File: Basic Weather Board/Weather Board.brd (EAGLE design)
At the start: 160 x 100 mm, 4 parts, among them U1 AT30TS75, U2 TMP101", U3 LPS331AP, U4 MPL3115A2

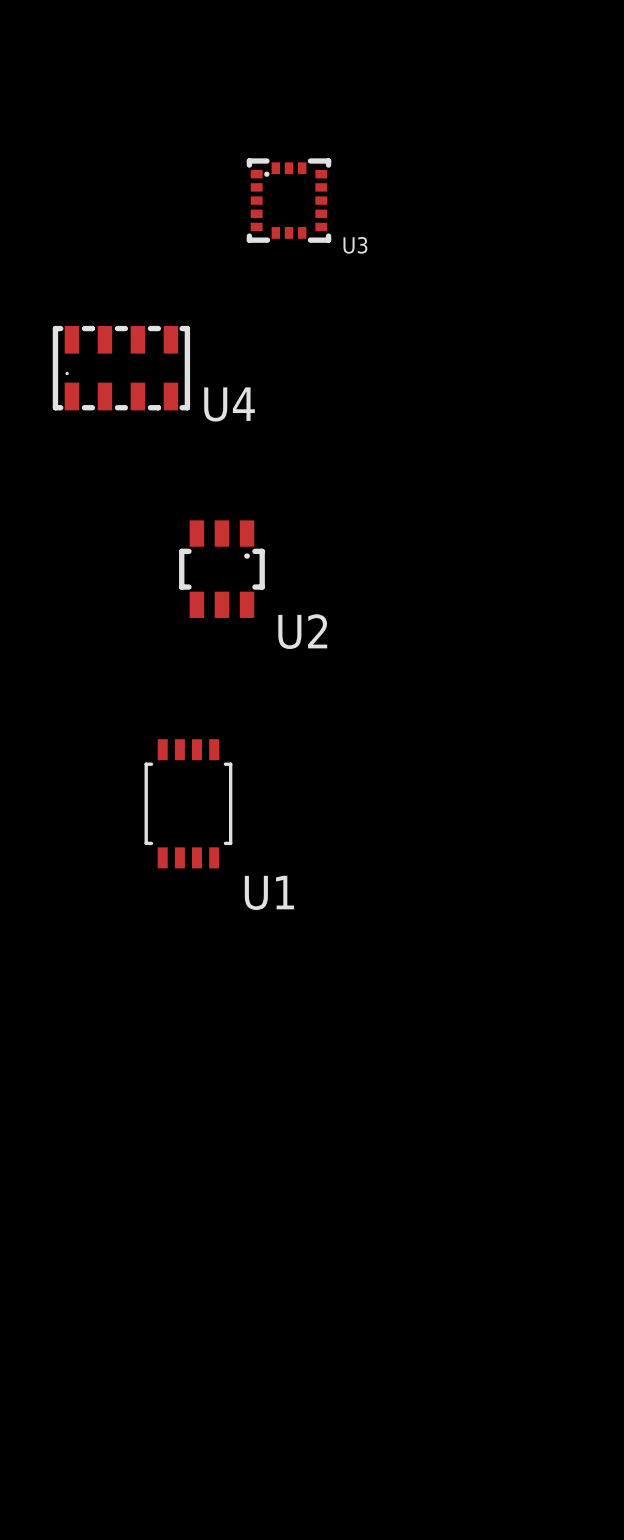
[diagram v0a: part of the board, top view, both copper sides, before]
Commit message: FRDM-KL25Z: Corrected parts to use Newark approved components and added missing componnets
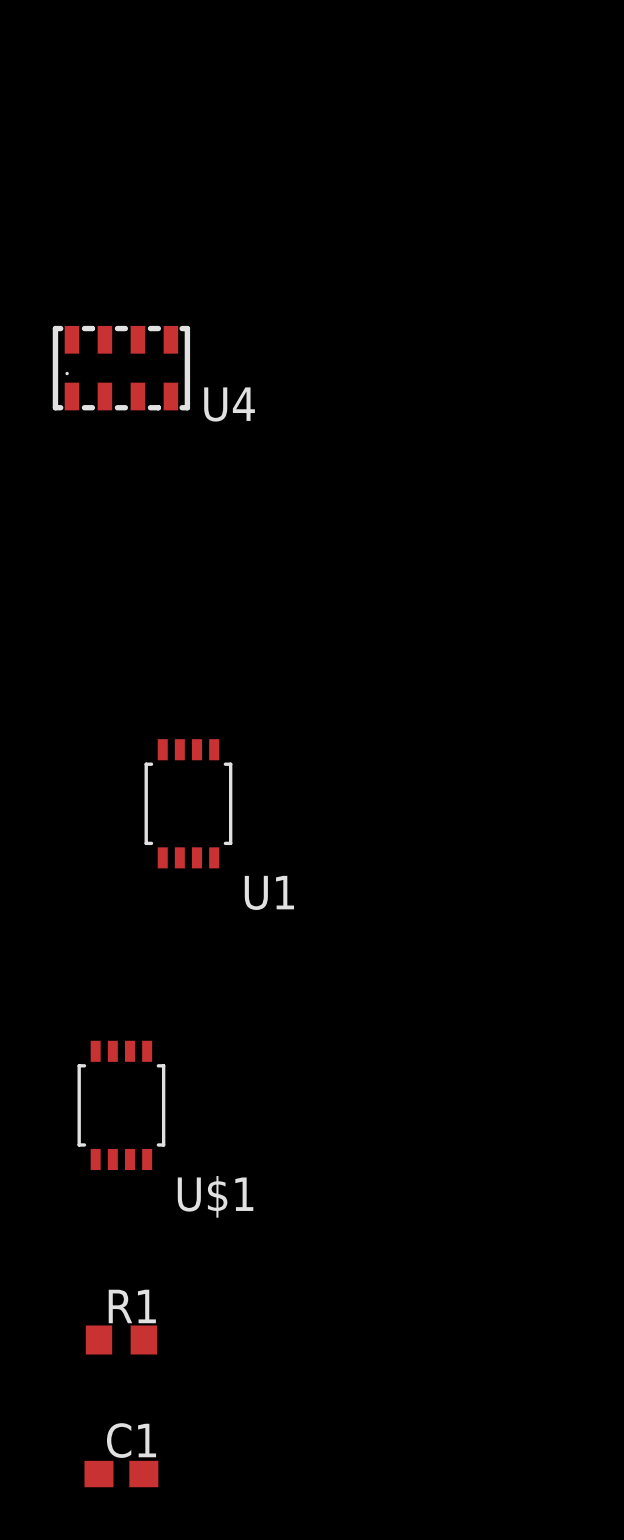
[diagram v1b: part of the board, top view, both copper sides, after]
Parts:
- removed U2: TMP101", Kas-Sensors:SOT23-6
- removed U3: LPS331AP, Kas-Sensors:LGA-16(3X3)
- added C1: 0.1uF, Kas-Capacitors:C0603
- added R1: 10k, Kas-Resistors:R0603
- added U$1: STCN75DS2F, Kas-Sensors:MSOP-8
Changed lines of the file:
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@@
 <layer number="48" name="Document" color="7" fill="1" visible="yes" active="yes"/>
 <layer number="49" name="Reference" color="7" fill="1" visible="yes" active="yes"/>
+<layer number="50" name="dxf" color="7" fill="1" visible="no" active="no"/>
 <layer number="51" name="tDocu" color="7" fill="1" visible="yes" active="yes"/>
 <layer number="52" name="bDocu" color="7" fill="1" visible="yes" active="yes"/>
+<layer number="53" name="tGND_GNDA" color="7" fill="9" visible="no" active="no"/>
+<layer number="54" name="bGND_GNDA" color="1" fill="9" visible="no" active="no"/>
+<layer number="56" name="wert" color="7" fill="1" visible="no" active="no"/>
 <layer number="91" name="Nets" color="2" fill="1" visible="no" active="no"/>
 <layer number="92" name="Busses" color="1" fill="1" visible="no" active="no"/>
@@
 <layer number="97" name="Info" color="7" fill="1" visible="no" active="no"/>
 <layer number="98" name="Guide" color="6" fill="1" visible="no" active="no"/>
+<layer number="100" name="Muster" color="7" fill="1" visible="no" active="no"/>
+<layer number="101" name="Patch_Top" color="12" fill="4" visible="no" active="yes"/>
+<layer number="102" name="Vscore" color="7" fill="1" visible="no" active="yes"/>
+<layer number="103" name="tMap" color="7" fill="1" visible="no" active="yes"/>
+<layer number="104" name="Name" color="16" fill="1" visible="no" active="yes"/>
+<layer number="105" name="tPlate" color="7" fill="1" visible="no" active="yes"/>
+<layer number="106" name="bPlate" color="7" fill="1" visible="no" active="yes"/>
+<layer number="107" name="Crop" color="7" fill="1" visible="no" active="yes"/>
+<layer number="116" name="Patch_BOT" color="9" fill="4" visible="no" active="yes"/>
+<layer number="121" name="_tsilk" color="7" fill="1" visible="no" active="yes"/>
+<layer number="122" name="_bsilk" color="7" fill="1" visible="no" active="yes"/>
+<layer number="125" name="_tNames" color="7" fill="1" visible="no" active="yes"/>
+<layer number="144" name="Drill_legend" color="7" fill="1" visible="no" active="yes"/>
+<layer number="151" name="HeatSink" color="7" fill="1" visible="no" active="yes"/>
+<layer number="200" name="200bmp" color="1" fill="10" visible="no" active="yes"/>
+<layer number="201" name="201bmp" color="2" fill="10" visible="no" active="yes"/>
+<layer number="202" name="202bmp" color="3" fill="10" visible="no" active="yes"/>
+<layer number="203" name="203bmp" color="4" fill="10" visible="no" active="yes"/>
+<layer number="204" name="204bmp" color="5" fill="10" visible="no" active="yes"/>
+<layer number="205" name="205bmp" color="6" fill="10" visible="no" active="yes"/>
+<layer number="206" name="206bmp" color="7" fill="10" visible="no" active="yes"/>
+<layer number="207" name="207bmp" color="8" fill="10" visible="no" active="yes"/>
+<layer number="208" name="208bmp" color="9" fill="10" visible="no" active="yes"/>
+<layer number="209" name="209bmp" color="7" fill="1" visible="no" active="yes"/>
+<layer number="210" name="210bmp" color="7" fill="1" visible="no" active="yes"/>
+<layer number="211" name="211bmp" color="7" fill="1" visible="no" active="yes"/>
+<layer number="212" name="212bmp" color="7" fill="1" visible="no" active="yes"/>
+<layer number="213" name="213bmp" color="7" fill="1" visible="no" active="yes"/>
+<layer number="214" name="214bmp" color="7" fill="1" visible="no" active="yes"/>
+<layer number="215" name="215bmp" color="7" fill="1" visible="no" active="yes"/>
+<layer number="216" name="216bmp" color="7" fill="1" visible="no" active="yes"/>
+<layer number="217" name="217bmp" color="18" fill="1" visible="no" active="no"/>
+<layer number="218" name="218bmp" color="19" fill="1" visible="no" active="no"/>
+<layer number="219" name="219bmp" color="20" fill="1" visible="no" active="no"/>
+<layer number="220" name="220bmp" color="21" fill="1" visible="no" active="no"/>
+<layer number="221" name="221bmp" color="22" fill="1" visible="no" active="no"/>
+<layer number="222" name="222bmp" color="23" fill="1" visible="no" active="no"/>
+<layer number="223" name="223bmp" color="24" fill="1" visible="no" active="no"/>
+<layer number="224" name="224bmp" color="25" fill="1" visible="no" active="no"/>
+<layer number="250" name="Descript" color="3" fill="1" visible="no" active="no"/>
+<layer number="251" name="SMDround" color="12" fill="11" visible="no" active="no"/>
+<layer number="254" name="cooling" color="7" fill="1" visible="no" active="yes"/>
 </layers>
 <board>
@@
 <elements>
 <element name="U1" library="Kas-Sensors" package="MSOP-8" value="AT30TS75" x="-24.13" y="7.62"/>
-<element name="U2" library="Kas-Sensors" package="SOT23-6" value="TMP101&quot;" x="-22.86" y="16.51"/>
-<element name="U3" library="Kas-Sensors" package="LGA-16(3X3)" value="LPS331AP" x="-20.32" y="30.48"/>
 <element name="U4" library="Kas-Sensors" package="LGA-8(5X3)" value="MPL3115A2" x="-26.67" y="24.13"/>
+<element name="U$1" library="Kas-Sensors" package="MSOP-8" value="STCN75DS2F" x="-26.67" y="-3.81"/>
+<element name="R1" library="Kas-Resistors" package="R0603" value="10k" x="-26.67" y="-12.7">
+<attribute name="MANUFACTURER" value="TE Connectivity" x="-26.67" y="-12.7" size="1.778" layer="27" display="off"/>
+<attribute name="TOLARANCE" value="1%" x="-26.67" y="-12.7" size="1.778" layer="27" display="off"/>
+<attribute name="VOLTAGE" value="50" x="-26.67" y="-12.7" size="1.778" layer="27" display="off"/>
+<attribute name="TEMPERATURE_COEFFICIENT" value="50ppm" x="-26.67" y="-12.7" size="1.778" layer="27" display="off"/>
+<attribute name="NEWARK_PART_NUMBER" value="51R8604" x="-26.67" y="-12.7" size="1.778" layer="27" display="off"/>
+<attribute name="MANUFACTURER_PART_NUMBER" value="CPF0603F10KC1" x="-26.67" y="-12.7" size="1.778" layer="27" display="off"/>
+</element>
+<element name="C1" library="Kas-Capacitors" package="C0603" value="0.1uF" x="-26.67" y="-17.78">
+<attribute name="MANUFACTURER" value="Murata" x="-26.67" y="-17.78" size="1.778" layer="27" display="off"/>
+<attribute name="TOLARANCE" value="10%" x="-26.67" y="-17.78" size="1.778" layer="27" display="off"/>
+<attribute name="DIELECTRIC" value="X7R" x="-26.67" y="-17.78" size="1.778" layer="27" display="off"/>
+<attribute name="VOLTAGE" value="25" x="-26.67" y="-17.78" size="1.778" layer="27" display="off"/>
+<attribute name="NEWARK-PAR_NUMBER" value="14T3317" x="-26.67" y="-17.78" size="1.778" layer="27" display="off"/>
+<attribute name="TEMPERATURE" value="-55 ~ 125" x="-26.67" y="-17.78" size="1.778" layer="27" display="off"/>
+<attribute name="MANUFACTURER_PART_NUMBER" value="GRM188R71E104KA01D" x="-26.67" y="-17.78" size="1.778" layer="27" display="off"/>
+</element>
 </elements>
 <signals>

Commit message: Weather Board Basic: Minor changes
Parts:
- added C2, C3: 0.1uF, Kas-Capacitors:C0603
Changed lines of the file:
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@@
 <attribute name="MANUFACTURER_PART_NUMBER" value="GRM188R71E104KA01D" x="-26.67" y="-17.78" size="1.778" layer="27" display="off"/>
+</element>
+<element name="C2" library="Kas-Capacitors" package="C0603" value="0.1uF" x="-26.67" y="-22.86">
+<attribute name="MANUFACTURER" value="Multicomp" x="-26.67" y="-22.86" size="1.778" layer="27" display="off"/>
+<attribute name="TOLARANCE" value="10%" x="-26.67" y="-22.86" size="1.778" layer="27" display="off"/>
+<attribute name="DIELECTRIC" value="X7R" x="-26.67" y="-22.86" size="1.778" layer="27" display="off"/>
+<attribute name="VOLTAGE" value="10" x="-26.67" y="-22.86" size="1.778" layer="27" display="off"/>
+<attribute name="NEWARK_PART_NUMBER" value="23T7300" x="-26.67" y="-22.86" size="1.778" layer="27" display="off"/>
+<attribute name="TEMPERATURE" value="-55 ~ 125" x="-26.67" y="-22.86" size="1.778" layer="27" display="off"/>
+<attribute name="MANUFACTURER_PART_NUMBER" value="MCSH18B104K100CT" x="-26.67" y="-22.86" size="1.778" layer="27" display="off"/>
+</element>
+<element name="C3" library="Kas-Capacitors" package="C0603" value="0.1uF" x="-26.67" y="-27.94">
+<attribute name="MANUFACTURER" value="Multicomp" x="-26.67" y="-27.94" size="1.778" layer="27" display="off"/>
+<attribute name="TOLARANCE" value="10%" x="-26.67" y="-27.94" size="1.778" layer="27" display="off"/>
+<attribute name="DIELECTRIC" value="X7R" x="-26.67" y="-27.94" size="1.778" layer="27" display="off"/>
+<attribute name="VOLTAGE" value="10" x="-26.67" y="-27.94" size="1.778" layer="27" display="off"/>
+<attribute name="NEWARK_PART_NUMBER" value="23T7300" x="-26.67" y="-27.94" size="1.778" layer="27" display="off"/>
+<attribute name="TEMPERATURE" value="-55 ~ 125" x="-26.67" y="-27.94" size="1.778" layer="27" display="off"/>
+<attribute name="MANUFACTURER_PART_NUMBER" value="MCSH18B104K100CT" x="-26.67" y="-27.94" size="1.778" layer="27" display="off"/>
 </element>
 </elements>
